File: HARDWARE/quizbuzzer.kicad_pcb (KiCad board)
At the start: 2 copper layers, 174 x 97.5 mm, 87 parts, among them J1 Controls, J10 Reciver 5, J11 Reciver 6, J12 Reciver 7, J13 Reciver 8, J14 Reciver 10, J15 Bulb1, J16 Bulb3, J17 Bulb3, J18 Bulb4, J19 Bulb5, J2 MP3out, J20 Bulb6, J21 Bulb7, J22 Bulb8, J23 Bulb9, J24 Bulb10, J25 Conn_02x14_Odd_Even, J26 DMX, J3 I2C, J4 Powerjack, J5 Reciver 1, J6 Reciver 2, J7 Reciver 3, J8 Reciver 4, J9 Reciver 9, K1 SANYOU_SRD_Form_A, K10 SANYOU_SRD_Form_A, K2 SANYOU_SRD_Form_A, K3 SANYOU_SRD_Form_A, K4 SANYOU_SRD_Form_A, K5 SANYOU_SRD_Form_A, K6 SANYOU_SRD_Form_A, K7 SANYOU_SRD_Form_A, K8 SANYOU_SRD_Form_A, K9 SANYOU_SRD_Form_A, Q1 2N3904, Q10 2N3904, Q2 2N3904, Q3 2N3904, Q4 2N3904, Q5 2N3904, Q6 2N3904, Q7 2N3904, Q8 2N3904, Q9 2N3904, U1 L7805, U2 MAX485E

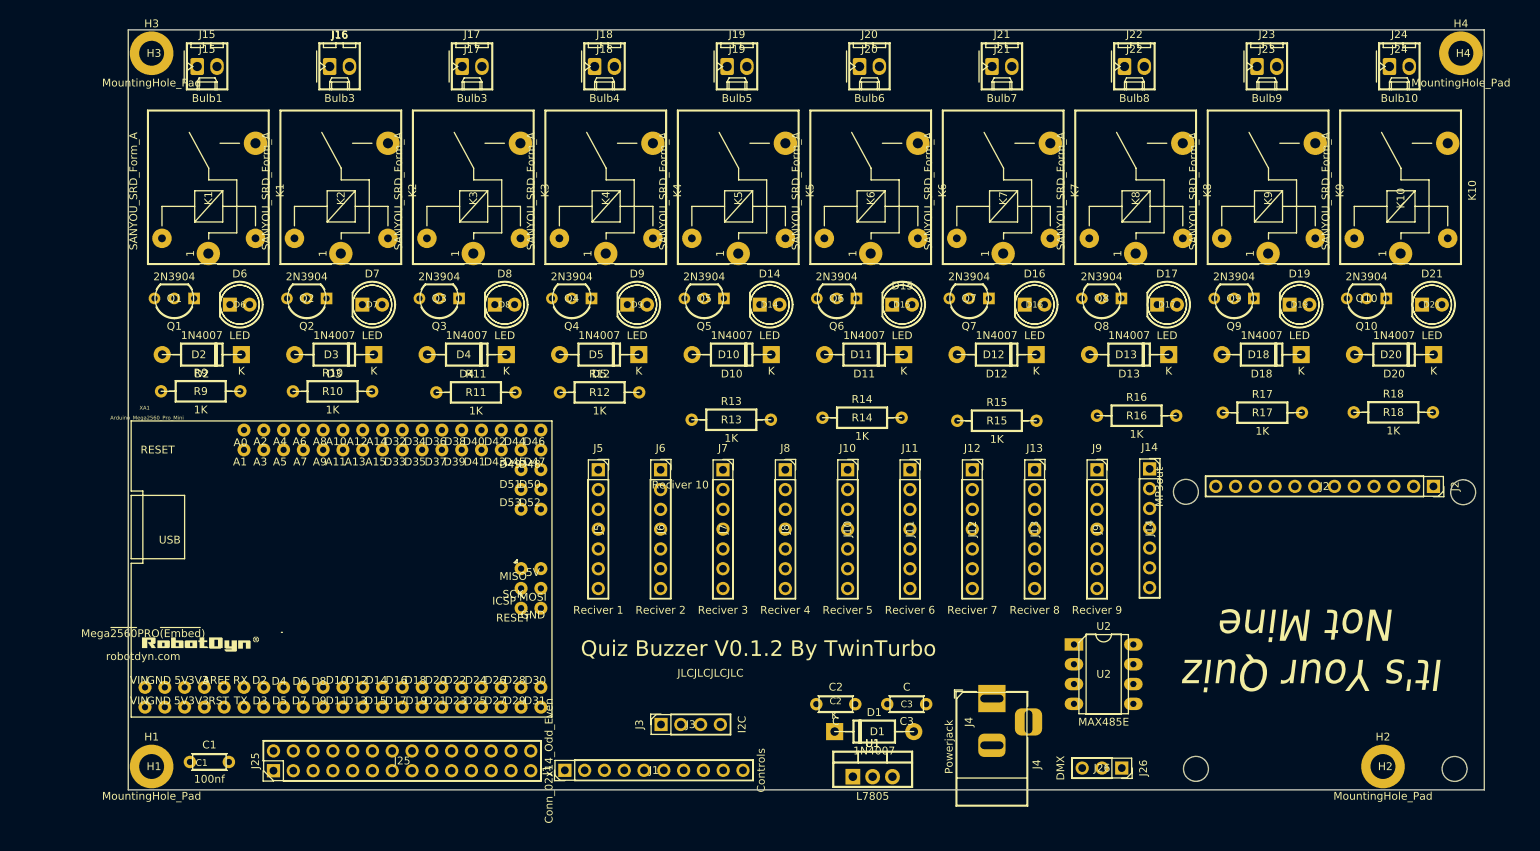
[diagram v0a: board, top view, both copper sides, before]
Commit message: Port Sort + 10 to 8 channel
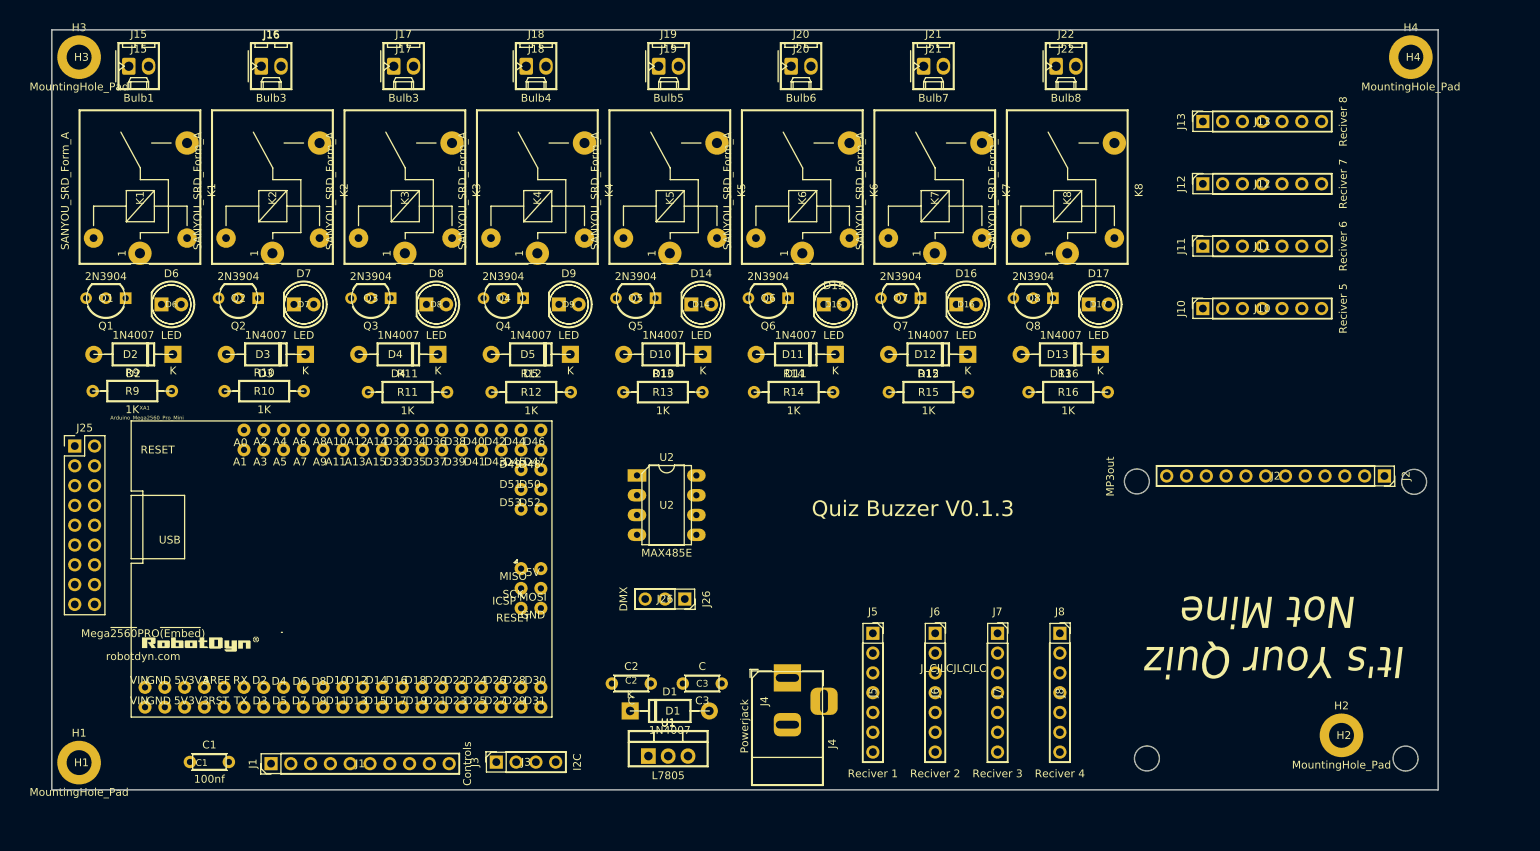
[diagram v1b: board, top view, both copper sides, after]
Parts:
- removed D18, D20: 1N4007, Diode_THT:D_DO-41_SOD81_P10.16mm_Horizontal
- removed D19, D21: LED, LED_THT:LED_D5.0mm
- removed J14: Reciver 10, Connector_PinSocket_2.54mm:PinSocket_1x07_P2.54mm_Vertical
- removed J23: Bulb9, Connector_Molex:Molex_KK-254_AE-6410-02A_1x02_P2.54mm_Vertical
- removed J24: Bulb10, Connector_Molex:Molex_KK-254_AE-6410-02A_1x02_P2.54mm_Vertical
- removed J9: Reciver 9, Connector_PinSocket_2.54mm:PinSocket_1x07_P2.54mm_Vertical
- removed K10, K9: SANYOU_SRD_Form_A, Relay_THT:Relay_SPST_SANYOU_SRD_Series_Form_A
- removed Q10, Q9: 2N3904, Package_TO_SOT_THT:TO-92_Inline_Wide
- removed R17, R18: 1K, Resistor_THT:R_Axial_DIN0207_L6.3mm_D2.5mm_P10.16mm_Horizontal
- J25: value Conn_02x14_Odd_Even -> Conn_02x09_Odd_Even; footprint Connector_PinHeader_2.54mm:PinHeader_2x14_P2.54mm_Vertical -> Connector_PinHeader_2.54mm:PinHeader_2x09_P2.54mm_Vertical
- moved U2 60.1 mm to (98.2, 70.6)
- moved J26 60.1 mm to (104.4, 86.4)
- moved J10 50.1 mm to (170.9, 49.2), turned to 90 degrees
- moved J13 49.6 mm to (170.9, 25.2), turned to 90 degrees
- moved J25 48.9 mm to (26.1, 66.8), turned to 0 degrees
- moved J11 47.3 mm to (170.9, 41.2), turned to 90 degrees
- moved J12 47.1 mm to (170.9, 33.2), turned to 90 degrees
- moved J5 41.0 mm to (128.5, 90.8)
- moved J6 41.0 mm to (136.5, 90.8)
- moved J7 41.0 mm to (144.5, 90.8)
- moved J8 41.0 mm to (152.5, 90.8)
- moved J1 37.7 mm to (51.3, 107.6)
- moved C2 26.4 mm to (95.0, 97.3)
- moved C3 26.4 mm to (109.1, 97.3)
- moved D1 26.4 mm to (97.4, 100.8)
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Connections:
- J2 pad 10: PORTB_8 -> PORTB_7
- J2 pad 3: PORTB_1 -> PORTB_0
- J2 pad 4: PORTB_2 -> PORTB_1
- J2 pad 5: PORTB_3 -> PORTB_2
- J2 pad 6: PORTB_4 -> PORTB_3
- J2 pad 7: PORTB_5 -> PORTB_4
- J2 pad 8: PORTB_6 -> PORTB_5
- J2 pad 9: PORTB_7 -> PORTB_6
- J25 pad 10: AUX-HEAD-18 -> AUX-HEAD-13
- J25 pad 12: AUX-HEAD-19 -> AUX-HEAD-14
- J25 pad 14: AUX-HEAD-21 -> AUX-HEAD-15
- J25 pad 16: AUX-HEAD-20 -> AUX-HEAD-16
- J25 pad 17: AUX-HEAD-9 -> GND
- J25 pad 18: AUX-HEAD-22 -> +5V
- J25 pad 2: AUX-HEAD-14 -> AUX-HEAD-9
- J25 pad 4: AUX-HEAD-15 -> AUX-HEAD-10
- J25 pad 6: AUX-HEAD-16 -> AUX-HEAD-11
- J25 pad 8: AUX-HEAD-17 -> AUX-HEAD-12
- XA1 pad A0: AUX-HEAD-5 -> AUX-HEAD-1
- XA1 pad A1: AUX-HEAD-6 -> AUX-HEAD-2
- XA1 pad A10: AUX-HEAD-15 -> AUX-HEAD-11
- XA1 pad A11: AUX-HEAD-16 -> AUX-HEAD-12
- XA1 pad A12: AUX-HEAD-17 -> AUX-HEAD-13
- XA1 pad A13: AUX-HEAD-18 -> AUX-HEAD-14
- XA1 pad A14: AUX-HEAD-19 -> AUX-HEAD-15
- XA1 pad A15: AUX-HEAD-20 -> AUX-HEAD-16
- XA1 pad A2: AUX-HEAD-7 -> AUX-HEAD-3
- XA1 pad A3: AUX-HEAD-8 -> AUX-HEAD-4
- XA1 pad A4: AUX-HEAD-9 -> AUX-HEAD-5
- XA1 pad A5: AUX-HEAD-10 -> AUX-HEAD-6
- XA1 pad A6: AUX-HEAD-11 -> AUX-HEAD-7
- XA1 pad A7: AUX-HEAD-12 -> AUX-HEAD-8
- XA1 pad A8: AUX-HEAD-13 -> AUX-HEAD-9
- XA1 pad A9: AUX-HEAD-14 -> AUX-HEAD-10
- XA1 pad D10: AUX-HEAD-27 -> PORTB_4
- XA1 pad D11: Lamp1 -> PORTB_5
- XA1 pad D12: Lamp2 -> PORTB_6
- XA1 pad D13: Lamp3 -> PORTB_7
- XA1 pad D14: AUX-HEAD-4 -> unconnected-(XA1-D14_TX3-PadD14)
- XA1 pad D15: AUX-HEAD-3 -> unconnected-(XA1-D15_RX3-PadD15)
- XA1 pad D16: AUX-HEAD-2 -> unconnected-(XA1-D16_TX2-PadD16)
- XA1 pad D17: AUX-HEAD-1 -> unconnected-(XA1-D17_RX2-PadD17)
- XA1 pad D22: Lamp4 -> Lamp1
- XA1 pad D23: Lamp5 -> Lamp2
- XA1 pad D24: Lamp6 -> Lamp3
- XA1 pad D25: Lamp7 -> Lamp4
- XA1 pad D26: Lamp8 -> Lamp5
- XA1 pad D27: Lamp9 -> Lamp6
- XA1 pad D28: Lamp10 -> Lamp7
- XA1 pad D29: Net-(J1-Pin_2) -> Lamp8
- XA1 pad D3: AUX-HEAD-24 -> unconnected-(XA1-D3_INT1-PadD3)
- XA1 pad D30: Net-(J1-Pin_3) -> Net-(J1-Pin_2)
- XA1 pad D31: Net-(J1-Pin_4) -> Net-(J1-Pin_3)
- XA1 pad D32: Net-(J1-Pin_5) -> Net-(J1-Pin_4)
- XA1 pad D33: Net-(J1-Pin_6) -> Net-(J1-Pin_5)
- XA1 pad D34: Net-(J1-Pin_7) -> Net-(J1-Pin_6)
- XA1 pad D35: Net-(J1-Pin_8) -> Net-(J1-Pin_7)
- XA1 pad D36: Net-(J1-Pin_9) -> Net-(J1-Pin_8)
- XA1 pad D37: Rec1 -> Net-(J1-Pin_9)
- XA1 pad D38: Rec2 -> unconnected-(XA1-PadD38)
- XA1 pad D39: Rec3 -> unconnected-(XA1-PadD39)
- XA1 pad D4: PORTB_1 -> unconnected-(XA1-PadD4)
- XA1 pad D40: Rec4 -> unconnected-(XA1-PadD40)
- XA1 pad D41: Rec5 -> unconnected-(XA1-PadD41)
- XA1 pad D42: Rec6 -> Rec1
- XA1 pad D43: Rec7 -> Rec2
- XA1 pad D44: Rec8 -> Rec3
- XA1 pad D45: Rec9 -> Rec4
- XA1 pad D46: Rec10 -> Rec5
- XA1 pad D47: AUX-HEAD-21 -> Rec6
- XA1 pad D48: AUX-HEAD-22 -> Rec7
- XA1 pad D49: AUX-HEAD-23 -> Rec8
- XA1 pad D5: PORTB_2 -> unconnected-(XA1-PadD5)
- XA1 pad D50: PORTB_5 -> PORTB_3
- XA1 pad D51: PORTB_6 -> PORTB_2
- XA1 pad D52: PORTB_7 -> PORTB_1
- XA1 pad D53: PORTB_8 -> PORTB_0
- XA1 pad D6: PORTB_3 -> unconnected-(XA1-PadD6)
- XA1 pad D7: PORTB_4 -> unconnected-(XA1-PadD7)
- XA1 pad D8: AUX-HEAD-25 -> unconnected-(XA1-PadD8)
- XA1 pad D9: AUX-HEAD-26 -> unconnected-(XA1-PadD9)
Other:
- board size 174 x 97.5 mm -> 177.9 x 97.5 mm
- board text added: "Quiz Buzzer V0.1.3"
- board text removed: "Quiz Buzzer V0.1.2 By TwinTurbo"

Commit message: Code sanitisation part 1
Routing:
- net GND: track 0.00 -> 686.6 mm
- net +5V: track 0.00 -> 540.3 mm
- net +12V: track 0.00 -> 212.6 mm
- net PORTB_5: track 0.00 -> 133.3 mm
- net MP3_EN: track 0.00 -> 130.1 mm
- net PORTB_4: track 0.00 -> 129.9 mm, vias 0 -> 1
- net Rec8: track 0.00 -> 128.7 mm
- net Rec7: track 0.00 -> 125.1 mm
- net PORTB_7: track 0.00 -> 124.0 mm
- net PORTB_6: track 0.00 -> 122.2 mm
- net PORTB_0: track 0.00 -> 115.1 mm
- net Rec6: track 0.00 -> 112.6 mm
- net PORTB_1: track 0.00 -> 105.4 mm
- net Rec5: track 0.00 -> 104.3 mm
- net PORTB_2: track 0.00 -> 103.7 mm
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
